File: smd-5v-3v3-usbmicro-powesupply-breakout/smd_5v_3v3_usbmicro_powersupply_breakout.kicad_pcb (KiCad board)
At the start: 2 copper layers, 32 x 48 mm, 13 parts, among them J1 USB_B_Micro, J2 THT 5V Jumper, J3 THT 3V3 Jumper, J4 SMD 5V Pad, J5 SMD 3V3 Pad, U1 LMS1585AIS-3.3

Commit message: Add project info silkscreen to pcb
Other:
- board text added: "5V & 3V3 USB Micro Power Supply Breakout Board v02"
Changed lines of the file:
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@@
+		)
+	)
+	(gr_text "5V & 3V3\nUSB Micro\nPower Supply\nBreakout\nBoard v02"
+		(at 165.25 138.25 0)
+		(layer "F.SilkS")
+		(effects
+			(font
+				(size 1 1)
+				(thickness 0.14)
+			)
+			(justify left bottom)
 		)
 	)

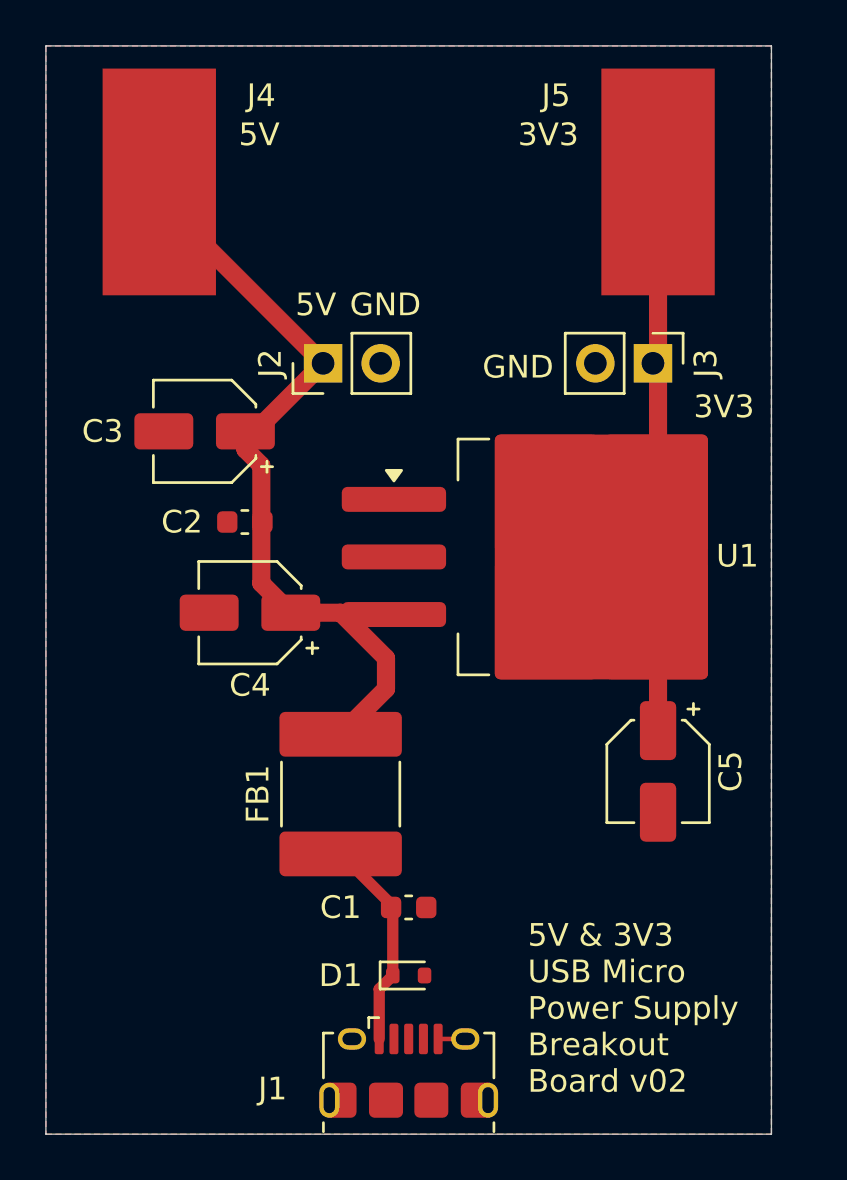
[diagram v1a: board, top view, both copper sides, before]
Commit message: v03 update (remove LDO input capacitor)
- LDO input capacitor isn't required as the pi-filter should reduce the
  ripples on the VBUS line giving us a "cleaner" 5V line therefore
  another input capacitor on the LDO isn't required (as there shouldn't
  be excessive rippling/noise)
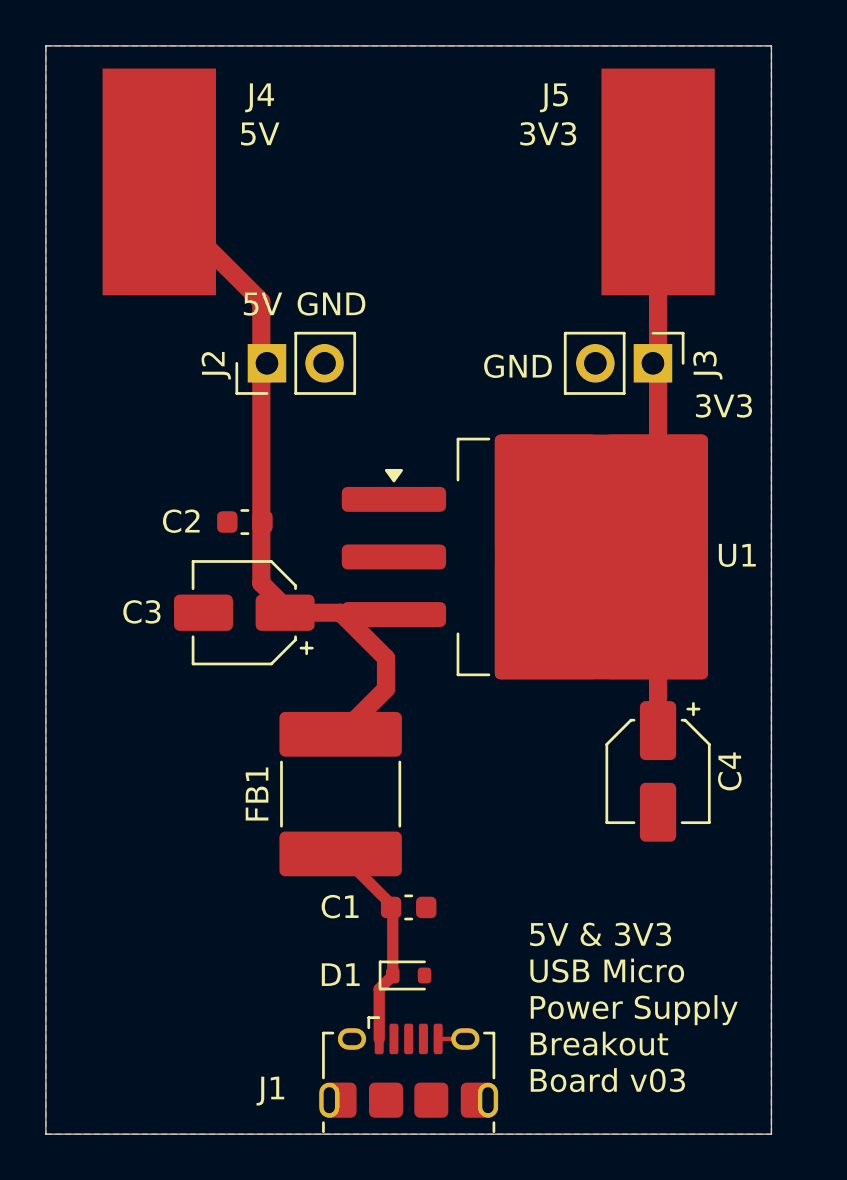
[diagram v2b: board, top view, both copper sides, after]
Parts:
- removed C5: 10u, Capacitor_SMD:CP_Elec_4x4.5
- moved C4 19.3 mm to (171.0, 124.0), turned to -90 degrees
- moved C3 8.19 mm to (152.8, 117.0)
- moved J2 2.47 mm to (153.8, 106.0)
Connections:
- C4 pad 1: +5V -> +3V3
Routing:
- net +5V: track 33.7 -> 30.6 mm
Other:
- board text added: "5V & 3V3 USB Micro Power Supply Breakout Board v03"
- board text removed: "5V & 3V3 USB Micro Power Supply Breakout Board v02"
